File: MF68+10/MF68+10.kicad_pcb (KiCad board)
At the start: 2 copper layers, 370.5 x 94.4 mm, 263 parts, among them U1 Teensy_3.2, U2 AN32183A

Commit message: Added PCB stabilizers to both 103 key and MF68+10
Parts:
- removed the REF** at (118.6, 64.8)
- removed the REF** at (157.7, 47.6)
- removed the REF** at (74.9, 77.2)
- removed the REF** at (128.0, 75.4)
- removed the REF** at (144.0, 75.2)
- removed the REF** at (159.5, 75.4)
- removed the REF** at (387.6, 84.5)
- removed the REF** at (397.6, 75.5)
- removed the REF** at (398.1, 93.0)
- removed the REF** at (393.6, 85.7)
- removed the REF** at (372.4, 74.2)
- removed the REF** at (372.4, 63.0)
- removed the REF** at (372.4, 59.0)
- removed the REF** at (379.1, 74.2)
- removed the REF** at (380.9, 59.0)
- removed the REF** at (397.6, 59.0)
- removed the REF** at (351.0, 36.0)
- removed the REF** at (303.0, 84.8)
- removed the REF** at (326.0, 89.2)
- removed the REF** at (318.2, 76.8)
- removed the REF** at (252.2, 97.2)
- added CHERRY: MX, Cherry:CHERRY_PCB_275H_STABILIZER, F.Cu at (331.0, 85.7)
- added CHERRY: MX, Cherry:CHERRY_PCB_225H_STABILIZER, F.Cu at (92.9, 85.7)
- added CHERRY: MX, Cherry:CHERRY_PCB_625H_STABILIZER, F.Cu at (202.4, 104.8)
- added CHERRY: MX, Cherry:CHERRY_PCB_225H_STABILIZER, F.Cu at (335.8, 66.7)
- added CHERRY: MX, Cherry:CHERRY_PCB_200H_STABILIZER, F.Cu at (338.1, 28.6)
- added REF**: GND Via, Cherry:GNDVia, F.Cu at (299.7, 76.2)
- added REF**: GND Via, Cherry:GNDVia, F.Cu at (314.3, 75.6)
- added REF**: GND Via, Cherry:GNDVia, F.Cu at (323.2, 66.7)
- added REF**: GND Via, Cherry:GNDVia, F.Cu at (314.3, 66.7)
- added REF**: GND Via, Cherry:GNDVia, F.Cu at (381.0, 67.3)
- added REF**: GND Via, Cherry:GNDVia, F.Cu at (375.3, 67.3)
- added REF**: GND Via, Cherry:GNDVia, F.Cu at (370.2, 67.3)
- added REF**: GND Via, Cherry:GNDVia, F.Cu at (361.3, 67.3)
- added REF**: GND Via, Cherry:GNDVia, F.Cu at (353.5, 75.4)
- moved R3 29.1 mm to (389.5, 93.2)
- moved R2 24.3 mm to (389.6, 90.4)
- moved R4 20.3 mm to (389.6, 78.4)
- moved D70 3.51 mm to (115.9, 99.2), turned to 270 degrees
- moved R1 3.22 mm to (306.8, 75.4)
- moved U2 3.00 mm to (309.4, 85.1)
- moved C1 2.35 mm to (302.5, 90.7)
- moved U1 0.13 mm to (360.4, 59.1), turned to 270 degrees
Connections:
- R1 pad 2: Net-(C1-Pad1) -> GND
- REF** pad GND: GND -> (no net) (x37)
- SW_X19Y4_66 pad SW1: (no net) -> C7
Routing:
- net C7: track 397.6 -> 529.7 mm, vias 4 -> 3
- net Z5: track 545.4 -> 652.7 mm, vias 4 -> 5
- net C8: track 382.2 -> 457.6 mm, vias 4 -> 3
- net R4: track 339.8 -> 413.6 mm, vias 1 -> 4
- net R5: track 337.9 -> 408.4 mm
- net C1: track 525.7 -> 594.7 mm, vias 5 -> 4
- net GND: track 111.6 -> 43.1 mm, vias 6 -> 2
- net R6: track 226.4 -> 286.4 mm, vias 0 -> 2
- net SDA: track 29.3 -> 78.2 mm
- net Z8: track 646.8 -> 605.1 mm, vias 6 -> 5
- net R7: track 200.5 -> 239.8 mm, vias 0 -> 2
- net SCL: track 29.3 -> 68.0 mm
- net C4: track 470.0 -> 507.5 mm, vias 3 -> 2
- net R8: track 176.9 -> 208.3 mm
- net C3: track 494.1 -> 523.8 mm, vias 1 -> 2
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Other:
- board text removed: "BLUE"
- board text removed: "GREEN"
- board text removed: "RED"

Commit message: Reworked RGB LED and added connector for off board LED.
Shrunk mounting holes and removed plating.
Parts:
- added REF**: GND Via, Cherry:GNDVia, F.Cu at (379.5, 76.5)
- added REF**: GND Via, Cherry:GNDVia, F.Cu at (385.0, 93.5)
- added REF**: GND Via, Cherry:GNDVia, F.Cu at (392.0, 76.5)
- added REF**: GND Via, Cherry:GNDVia, F.Cu at (387.0, 76.5)
- added REF**: GND Via, Cherry:GNDVia, F.Cu at (392.0, 96.0)
- added REF**: GND Via, Cherry:GNDVia, F.Cu at (397.0, 76.0)
- added REF**: GND Via, Cherry:GNDVia, F.Cu at (397.0, 111.0)
- added REF**: Pin_Header_Straight_1x04, Pin_Headers:Pin_Header_Straight_1x04, F.Cu at (396.2, 85.1)
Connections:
- REF** pad : GND -> (no net)
- REF** pad 1: GND -> (no net) (x2)
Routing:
- net Net-(R3-Pad1): track 6.68 -> 17.5 mm
- net Z6: track 753.0 -> 744.3 mm
- net +5V: track 101.5 -> 109.3 mm
- net Net-(R2-Pad1): track 3.17 -> 8.81 mm
- net Net-(R4-Pad1): track 11.5 -> 15.1 mm
- net R8: track 208.3 -> 210.4 mm
- net Net-(D17-Pad1): track 145.2 -> 146.3 mm
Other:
- board text added: "+"
- board text added: "B"
- board text added: "G"
- board text added: "R"

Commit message: Trace cleanup
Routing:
- net C7: track 529.7 -> 421.0 mm, vias 3 -> 4
- net R4: track 413.6 -> 396.1 mm, vias 4 -> 2
- net C3: track 523.8 -> 511.2 mm
- net C8: track 457.6 -> 445.7 mm, vias 3 -> 2
- net C4: track 507.5 -> 500.2 mm, vias 2 -> 3

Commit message: Final commit for order placed on 6/23/2016
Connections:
- REF** pad GND: (no net) -> GND (x37)
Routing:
- net C8: track 445.7 -> 444.4 mm
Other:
- outline, holes or cut-outs redrawn
- board text added: "/u/ca178858"
- board text removed: "scott.t.wilson@gmail.com /u/ca178858"

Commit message: Moved diodes out of the way of the cherry stabilizers
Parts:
- removed the REF** at (241.1, 109.5)
- moved D65 26.2 mm to (340.0, 99.3)
- moved D54 16.8 mm to (100.3, 77.2), turned to 180 degrees
- moved D39 16.8 mm to (95.5, 58.2), turned to 180 degrees
- moved D51 10.7 mm to (316.2, 60.7)
- moved D16 8.43 mm to (320.5, 33.0)
- moved REF** 3.77 mm to (234.4, 110.7)
- moved REF** 0.54 mm to (313.9, 75.2)
- moved D72 0.51 mm to (193.0, 99.3), turned to 180 degrees
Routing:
- net R6: track 286.4 -> 351.1 mm
- net R9: track 193.0 -> 214.1 mm, vias 1 -> 2
- net Net-(D65-Pad2): track 6.44 -> 23.7 mm
- net Net-(D72-Pad2): track 6.37 -> 22.4 mm
- net Net-(D51-Pad2): track 6.58 -> 20.6 mm
- net Net-(D54-Pad2): track 6.56 -> 18.4 mm, vias 0 -> 1
- net Net-(D39-Pad2): track 6.63 -> 14.2 mm
- net Net-(D16-Pad2): track 13.3 -> 19.5 mm
- net R3: track 369.2 -> 366.0 mm
- net SDA: track 78.2 -> 76.1 mm
- net R8: track 210.4 -> 209.0 mm
- net R5: track 408.4 -> 409.3 mm
- net R10: track 101.6 -> 102.3 mm
- net NSRT: track 78.7 -> 79.4 mm

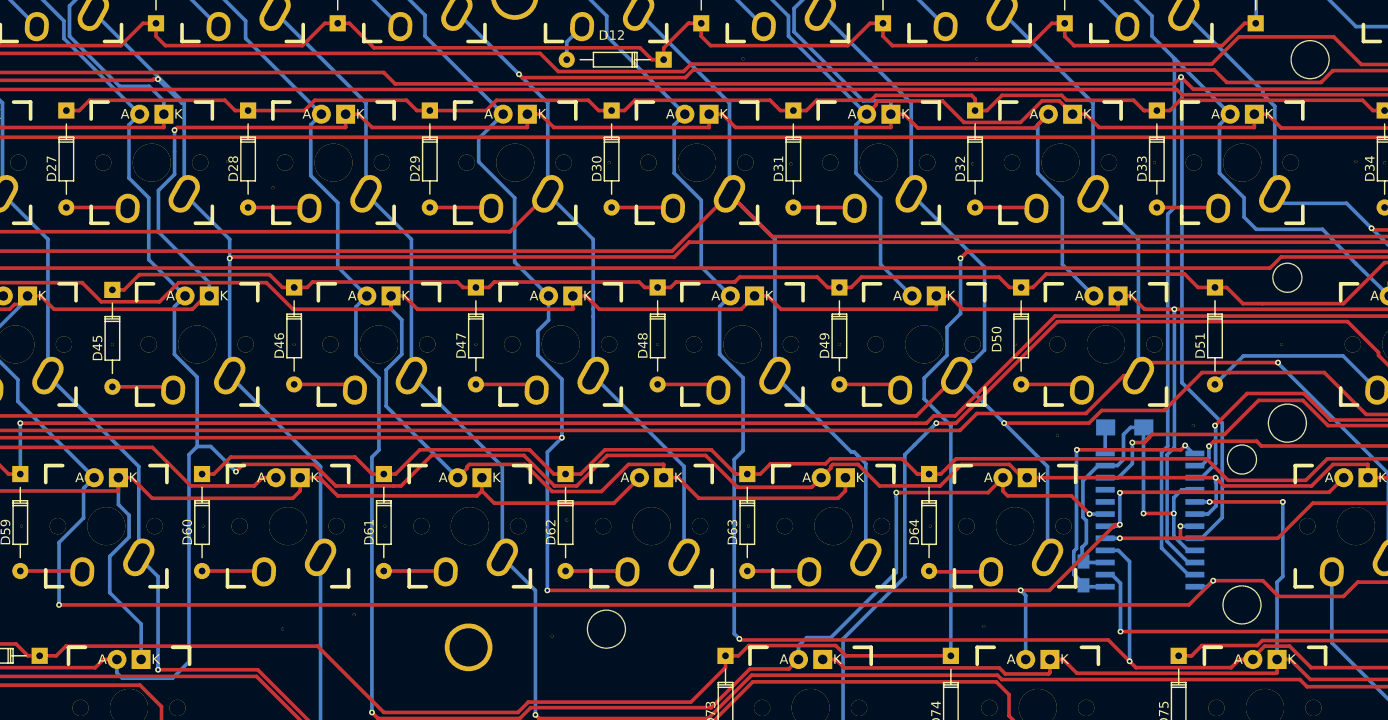
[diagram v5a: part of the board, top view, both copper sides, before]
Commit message: Renamed BlueWeevil to LFK78
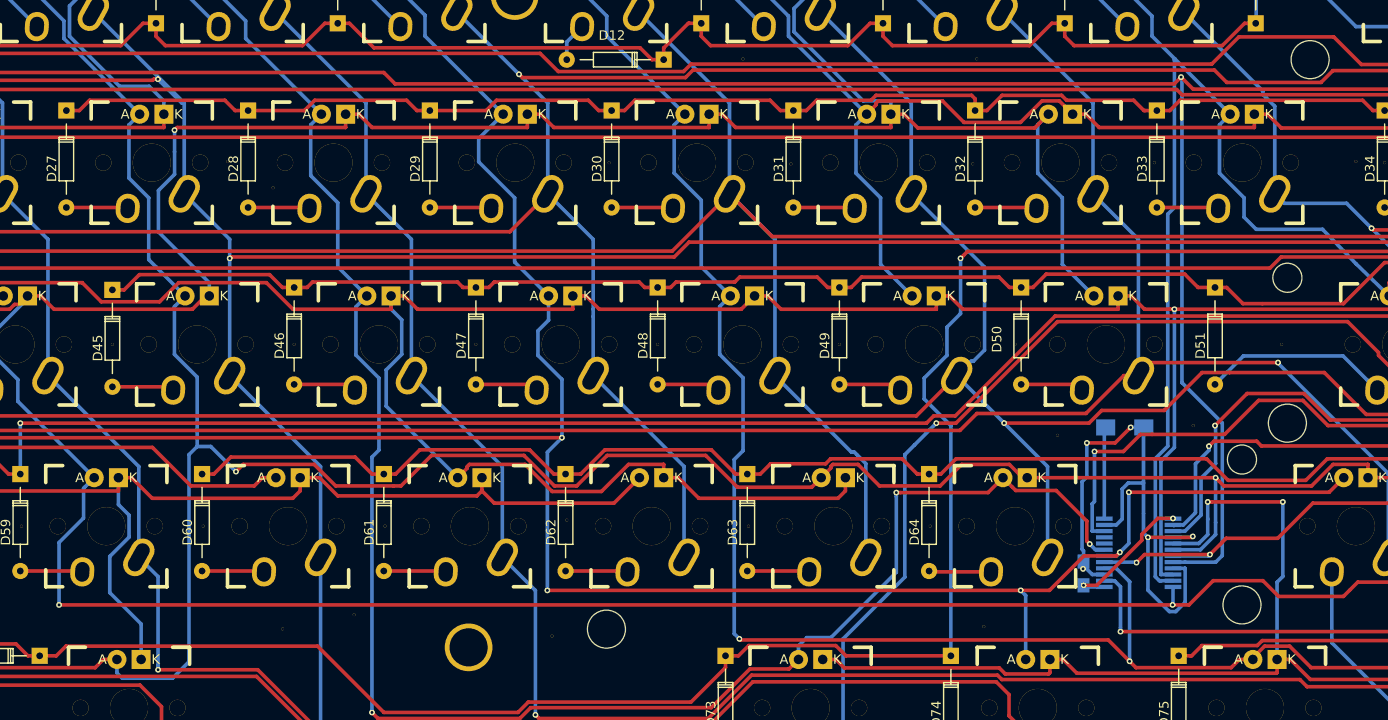
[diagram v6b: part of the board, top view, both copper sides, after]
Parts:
- C1: value C -> 1µF
- R1: value R -> 39kΩ
- R2: value R2 -> 150Ω
- R3: value R3 -> 120Ω
- R4: value R4 -> 120Ω
- U2: footprint Housings_SOIC:SOIC-24_7.5x15.4mm_Pitch1.27mm -> Housings_SSOP:SSOP-24_5.3x8.2mm_Pitch0.65mm
- moved U2 3.63 mm to (308.2, 88.5)
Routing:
- net GND: track 43.1 -> 65.1 mm, vias 2 -> 5
- net Net-(C1-Pad1): track 30.4 -> 14.9 mm
- net NSRT: track 79.4 -> 87.1 mm
- net SCL: track 68.0 -> 75.5 mm
- net Net-(R1-Pad1): track 2.75 -> 9.63 mm
- net SDA: track 76.1 -> 83.0 mm
- net Z10: track 154.9 -> 161.2 mm
- net Z8: track 605.1 -> 610.8 mm
- net Z9: track 564.3 -> 569.8 mm
- net Z3: track 543.0 -> 540.4 mm
- net +5V: track 109.3 -> 111.5 mm
- net Z1: track 504.7 -> 506.5 mm
- net Z2: track 651.6 -> 652.9 mm
- net Z7: track 561.8 -> 563.0 mm
- net Z6: track 744.3 -> 744.9 mm
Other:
- net class Default: clearance 0.2032 -> 0.1524
- rule trace_clearance: 0.2032 -> 0.1524
- rule trace_min: 0.254 -> 0.01524
- rule via_min_size: 0.6096 -> 0.03048
